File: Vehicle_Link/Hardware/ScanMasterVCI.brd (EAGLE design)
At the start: 53 x 39.4 mm, 86 parts, among them IC1 XMEGA32A4U, IC2 TL331, P1 HARFLEX-1515012-601, Q1 RUM002N05, Q10 ZXMP6A17G, Q3 RUM002N05, Q4 RUM002N05, Q5 RRF015P03, Q6 RUM002N05, Q7 RRF015P03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

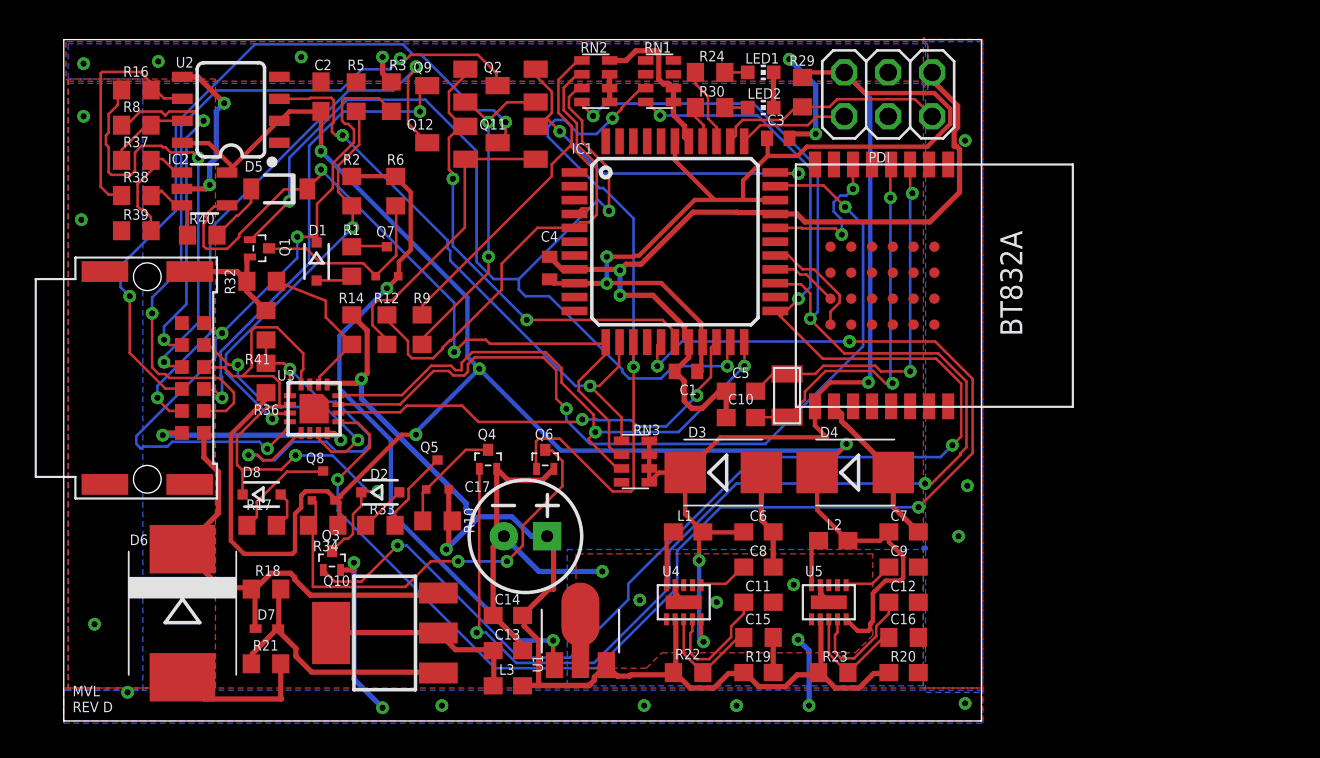
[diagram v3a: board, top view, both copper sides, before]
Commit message: Added OBD connector board section, along with proper connectors so I don't have to solder wires anymore. Still need to add milling marks
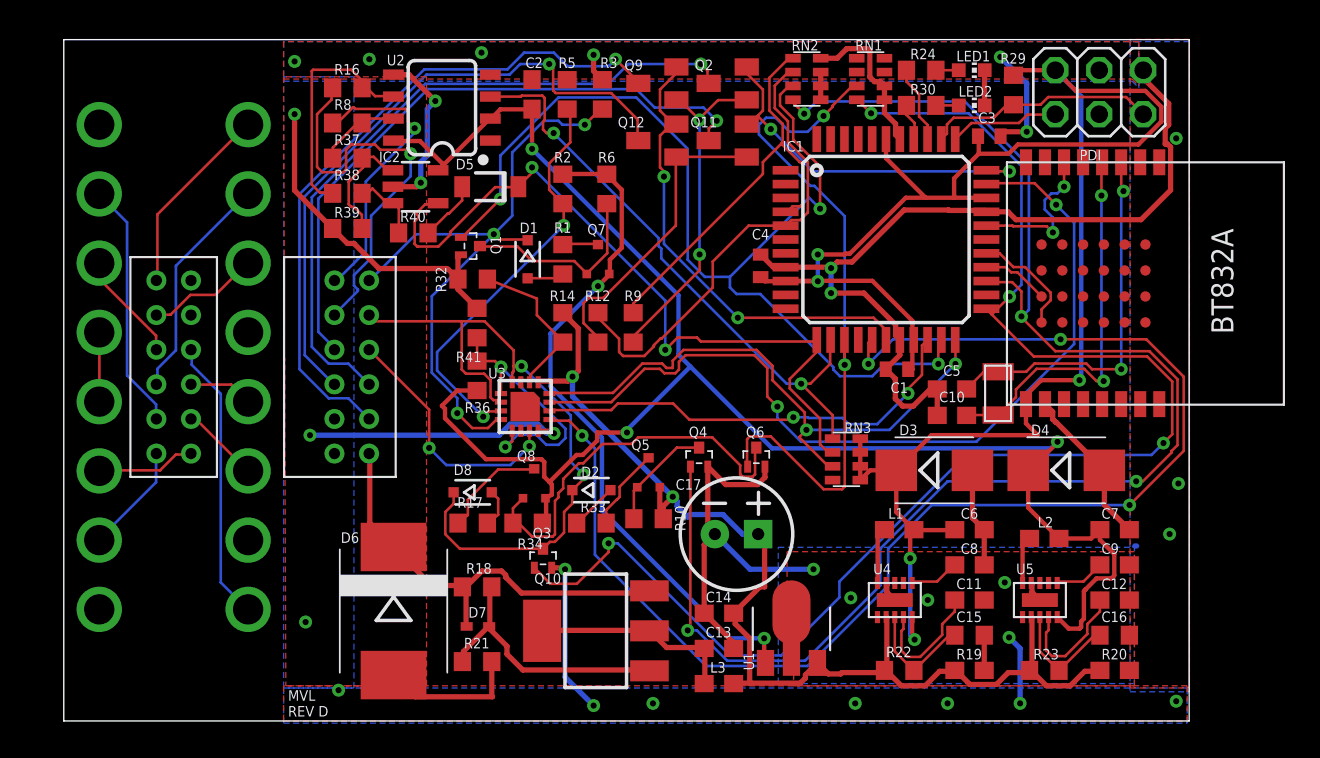
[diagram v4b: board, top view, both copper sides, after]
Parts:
- removed P1: HARFLEX-1515012-601, customics:HARFLEX-1515012-601
- added C18: J1962M, customics:J1962M
- added U$1: DF11-12DP-2DS, customics:DF11-12DP-2DS
- added U$2: DF11-12DS-2DS, customics:DF11-12DS-2DSA
- moved Q4 12.2 mm to (36.7, 15.2)
- moved Q6 12.2 mm to (40.0, 15.2)
- moved D5 12.2 mm to (24.6, 30.9)
- moved D7 12.2 mm to (23.9, 5.46)
- moved R18 12.2 mm to (23.9, 7.75)
- moved R21 12.2 mm to (23.9, 3.43)
- moved R36 12.2 mm to (23.9, 19.9)
- moved R40 12.2 mm to (20.2, 28.2)
- moved R41 12.2 mm to (23.9, 23.0)
- moved U2 12.2 mm to (21.8, 35.4)
- moved U3 12.2 mm to (26.7, 18.2)
- moved C1 12.2 mm to (48.1, 20.3)
- moved C10 12.2 mm to (51.3, 17.7)
- moved C11 12.2 mm to (52.3, 6.99)
- moved C12 12.2 mm to (60.7, 6.99)
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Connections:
- new net N$14: C18.16, U$2.P$6
- new net N$25: C18.15, U$2.P$3
- new net N$28: C18.14, U$2.P$5
- new net N$29: C18.6, U$2.P$4
- new net N$32: C18.7, U$2.P$2
- new net N$40: C18.4, C18.5
- new net N$41: C18.3, U$2.P$7
- new net N$42: C18.9, U$2.P$10
- new net N$43: C18.12, U$2.P$9
- new net N$44: C18.11, U$2.P$8
- new net N$46: C18.2, U$2.P$1
- net GND: now also U$1.P$12; no longer P1.7, P1.NC1, P1.NC2, P1.NC3, P1.NC4
- net J1962-11: now also U$1.P$8; no longer P1.10
- net J1962-12: now also U$1.P$9; no longer P1.9
- net J1962-14: now also U$1.P$5; no longer P1.4
- net J1962-15: now also U$1.P$3; no longer P1.2
- net J1962-16: now also U$1.P$6; no longer P1.6
- net J1962-2: now also U$1.P$1; no longer P1.1
- net J1962-3: now also U$1.P$7; no longer P1.11
- net J1962-6: now also U$1.P$4; no longer P1.5
- net J1962-7: now also U$1.P$2; no longer P1.3
- net J1962-9: now also U$1.P$10; no longer P1.8
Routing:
- net N$42: track 0.00 -> 16.4 mm
- net GND: track 166.9 -> 182.4 mm, vias 31 -> 30
- net N$32: track 0.00 -> 14.4 mm
- net N$25: track 0.00 -> 13.2 mm
- net J1962-14: track 26.9 -> 39.4 mm, vias 2 -> 1
- net N$14: track 0.00 -> 11.3 mm
- net N$6: track 23.1 -> 15.6 mm
- net +5V: track 103.4 -> 96.3 mm, vias 4 -> 3
- net N$28: track 0.00 -> 6.54 mm
- net N$29: track 0.00 -> 6.36 mm
- net N$46: track 0.00 -> 6.36 mm
- net J1962-12: track 42.9 -> 36.9 mm, vias 2 -> 1
- net N$41: track 0.00 -> 5.73 mm
- net N$44: track 0.00 -> 4.55 mm
- net N$40: track 0.00 -> 4.00 mm
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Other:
- board size 53 x 39.4 mm -> 65 x 39.4 mm

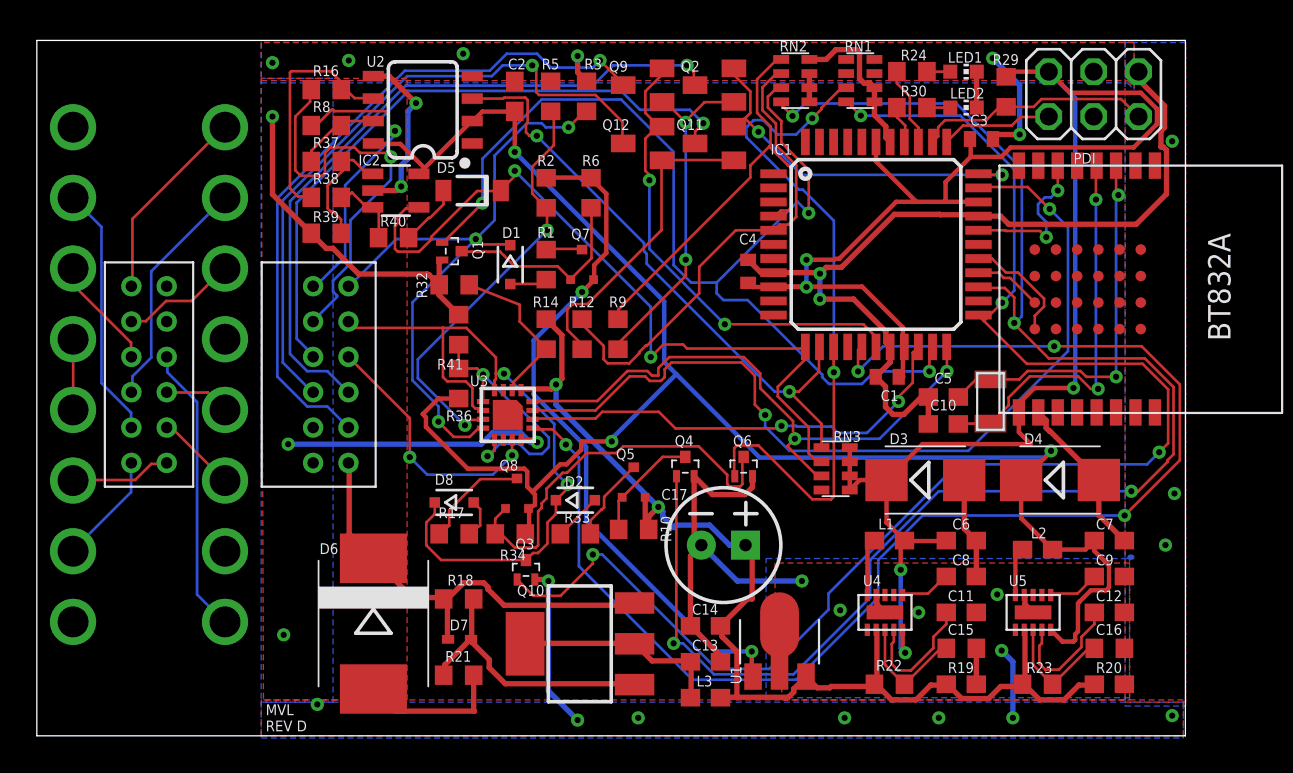
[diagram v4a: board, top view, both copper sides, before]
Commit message: Finished adding milling marks to the OBD connector PCB. Missed a ground connection on the OBD board, added it.
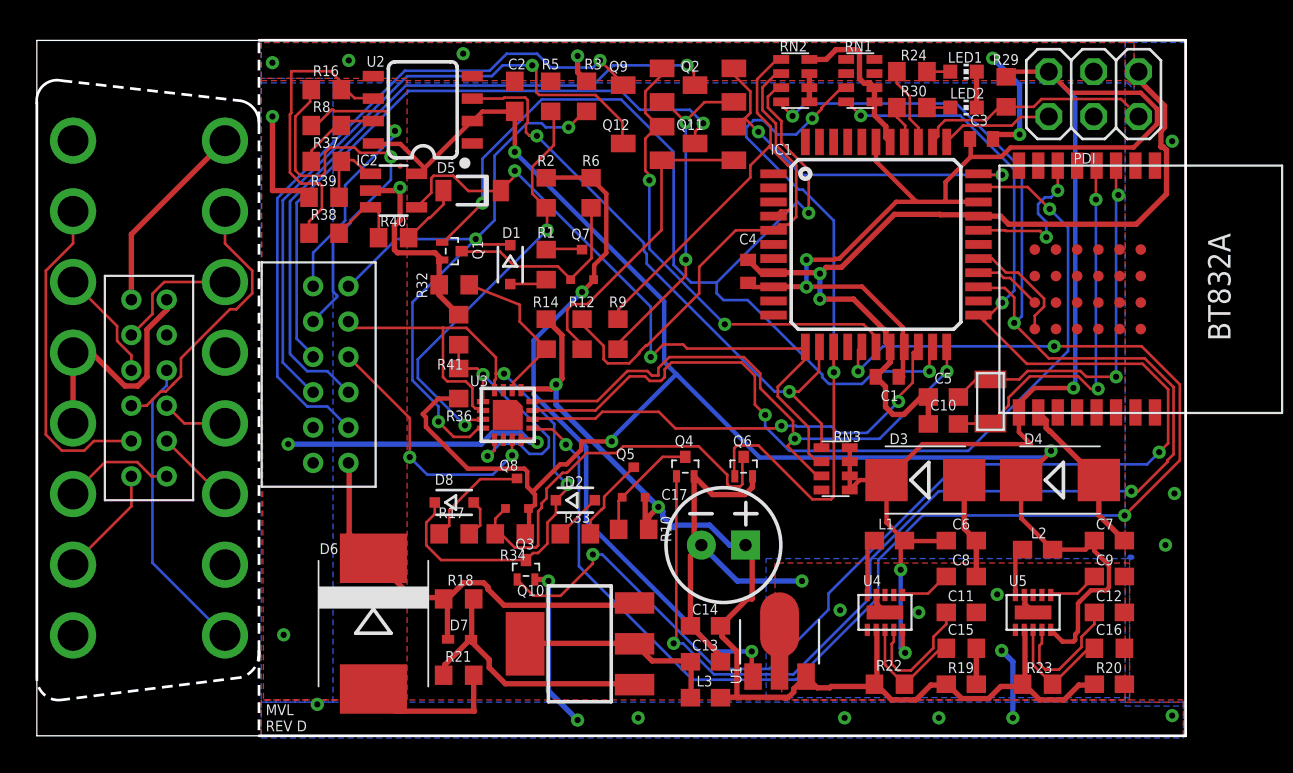
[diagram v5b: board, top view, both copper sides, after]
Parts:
- moved R38 2.04 mm to (16.3, 28.4)
- moved R39 2.04 mm to (16.3, 30.5)
- moved C18 0.76 mm to (6.35, 19.7)
- moved U$2 0.76 mm to (6.35, 19.7)
- moved IC2 0.13 mm to (20.2, 30.9)
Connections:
- net N$14 renamed CVBATT
- removed net N$40: C18.4, C18.5
- new net CGND: C18.4, C18.5, U$2.P$12
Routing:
- net CGND: track 0.00 -> 14.0 mm
- net GND: track 182.4 -> 171.3 mm, vias 30 -> 29
- net CCD-RX: track 43.7 -> 39.0 mm
- net N$32: track 14.4 -> 18.7 mm
- net N$40: track 4.00 -> 0.00 mm
- net N$34: track 6.95 -> 4.09 mm
- net N$33: track 13.6 -> 16.4 mm
- net N$25: track 13.2 -> 15.4 mm
- net N$28: track 6.54 -> 7.21 mm
- net N$42: track 16.4 -> 17.0 mm
- net N$41: track 5.73 -> 6.38 mm
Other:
- outline, holes or cut-outs redrawn

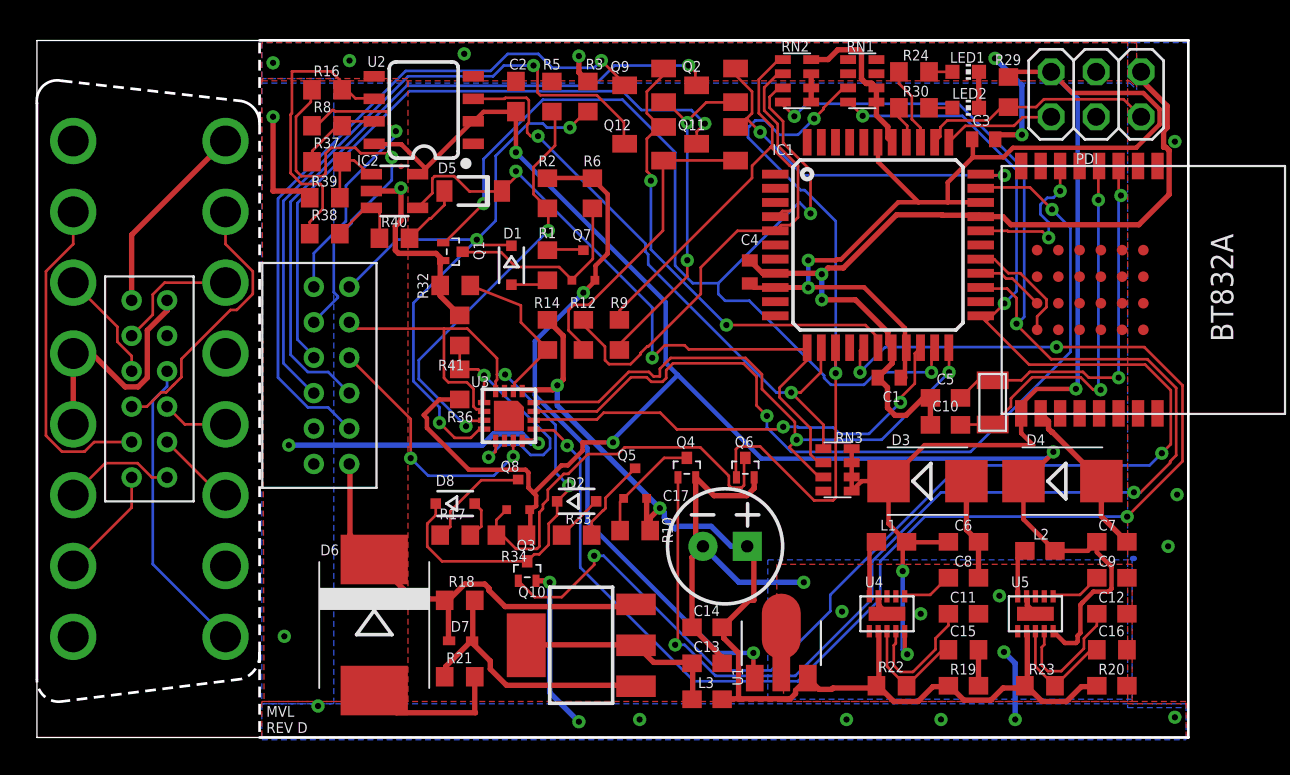
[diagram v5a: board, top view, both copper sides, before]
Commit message: Noticed an issue on the OBD connector. Pins didn't match to main board. Besides that final touches before I order boards, minimized vias and re-routed some traces that were just routed strangely
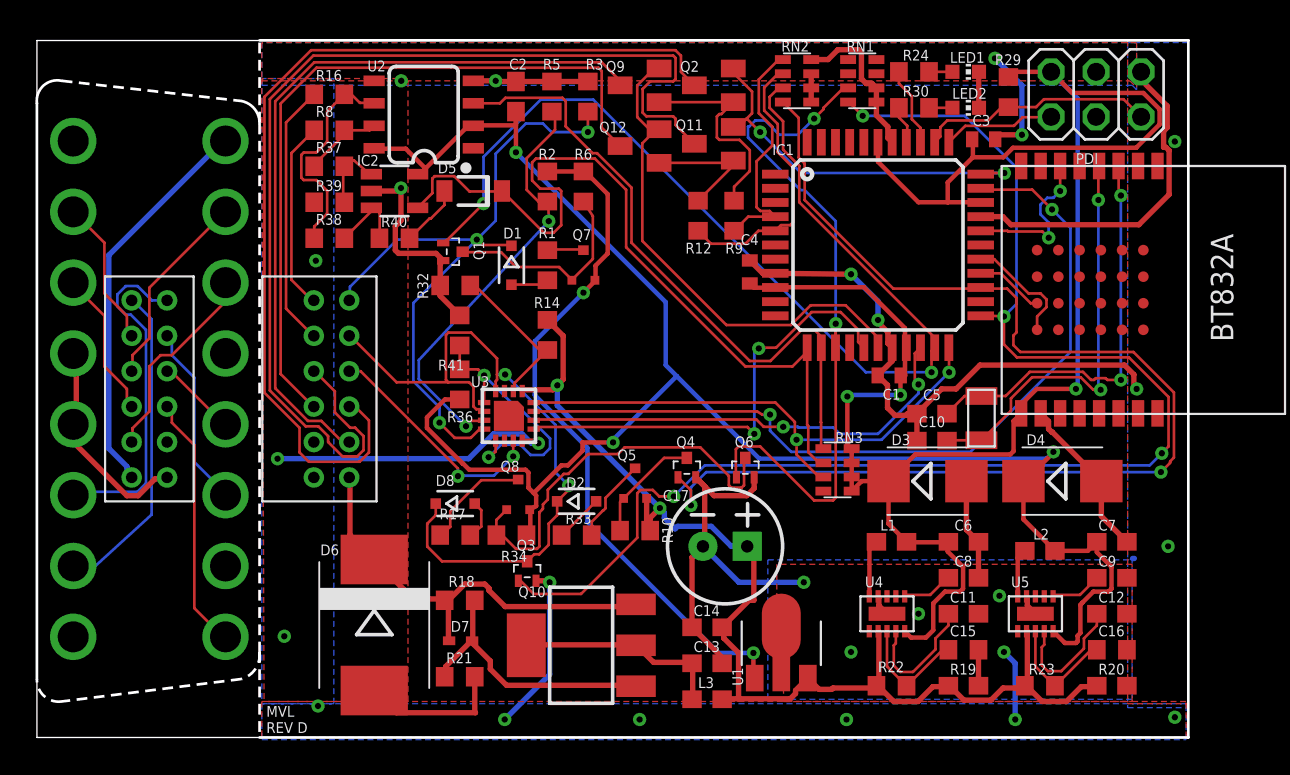
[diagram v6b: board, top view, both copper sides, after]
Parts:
- moved R12 9.34 mm to (37.3, 29.5), turned to 90 degrees
- moved R9 9.34 mm to (39.4, 29.5), turned to 90 degrees
- moved C10 1.17 mm to (50.5, 16.8)
- moved C5 1.17 mm to (50.5, 18.3)
- moved O1 1.09 mm to (53.3, 18.0)
- moved U$1 0.76 mm to (16.6, 19.7)
- moved R6 0.63 mm to (30.9, 31.1)
- moved R2 0.38 mm to (28.8, 31.1)
- moved R38 0.36 mm to (16.5, 28.2)
- moved R39 0.36 mm to (16.5, 30.2)
- moved R16 0.28 mm to (16.5, 36.3)
- moved R37 0.28 mm to (16.5, 32.3)
- moved R8 0.28 mm to (16.5, 34.3)
- moved Q12 0.28 mm to (34.0, 33.4)
- moved Q9 0.25 mm to (34.0, 36.8)
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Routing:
- net SCI-TRANS-RX: track 78.1 -> 25.6 mm, vias 4 -> 2
- net J1962-12: track 36.9 -> 62.0 mm, vias 1 -> 0
- net ISO-K-EN: track 88.4 -> 67.9 mm, vias 4 -> 2
- net J1962-6: track 39.8 -> 55.7 mm, vias 1 -> 0
- net N$41: track 6.38 -> 19.2 mm
- net N$46: track 6.37 -> 18.2 mm
- net SCI-B-EN: track 27.6 -> 15.8 mm
- net CVBATT: track 11.2 -> 22.3 mm
- net SCI-A-EN: track 24.5 -> 13.7 mm
- net N$5: track 17.8 -> 7.33 mm
- net N$32: track 18.7 -> 8.41 mm
- net J1962-11: track 23.4 -> 15.0 mm, vias 1 -> 0
- net N$1: track 19.5 -> 12.0 mm, vias 2 -> 0
- net CCD-RX: track 39.0 -> 45.7 mm, vias 2 -> 0
- net J1962-3: track 16.7 -> 10.7 mm, vias 1 -> 0
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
